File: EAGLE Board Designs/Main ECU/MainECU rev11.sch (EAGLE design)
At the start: 208 parts, among them J1 CONNECTOR-40__, J2 ADIS16460, J3 CONNECTOR-40__, J4 CONNECTOR-40__, J5 CONNECTOR-40__, K1 RELAY_DPDT_RT424024, K10 RELAY_DPDT_RT424024, K11 RELAY_DPDT_RT424024, K12 RELAY_DPDT_RT424024, K9 RELAY_DPDT_RT424024, Q3 TRANSISTOR_P_MOS_SOT-23_DMP30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, Q4 TRANSISTOR_N_MOS__DMG3406L-7, Q5 TRANSISTOR_P_MOS_SOT-23_DMP30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, Q6 TRANSISTOR_N_MOS__DMG3406L-7, U1 VOLTAGE_REGULATOR_SOT-223_3.3V, U2 TCAN1051HQV-Q1, U23 ADC128S022, U3 TCAN1051HQV-Q1, U32 ADC128S022, U33 TCAN1051HQV-Q1, U34 OPAMP_1_CHANNEL_OPA991, U37 OPAMP_1_CHANNEL_OPA991, U38 LOGICGATE_OR, U39 OPAMP_1_CHANNEL_OPA991, U4 TCAN1051HQV-Q1, U41 OPAMP_1_CHANNEL_OPA991, U42 LOGICGATE_OR, U43 OPAMP_1_CHANNEL_OPA991, U44 LOGICGATE_NAND, U45 TCAN1051HQV-Q1, U46 TCAN1051HQV-Q1, U5 ADM8316WBX30, U6 ADC128S022, U7 ADC128S022

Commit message: everything except LEDs
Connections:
- new net !AD4_CS: A3.D33, U32.!CS!
- net !AD3_CS: no longer A3.(CS)D10, U32.!CS!
- net +24V: now also J1.15, J1.16; no longer J1.1, J1.2
- net +5V: now also J1.14; no longer J1.3, J1.4
- net CANH_1: now also J1.12; no longer J1.16
- net CANH_2: now also J1.8; no longer J1.12
- net CANH_3: now also J1.4; no longer J1.8
- net CANL_1: now also J1.10; no longer J1.14
- net CANL_2: now also J1.6; no longer J1.10
- net CANL_3: now also J1.2; no longer J1.6
- net GND: now also J1.1, J1.3, J3.3, J3.4; no longer J1.15
- net REFERENCE: now also U32.IN2
- net SHDN_F: now also J3.1, J3.2
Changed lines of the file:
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@@
 <attribute name="DESCRIPTION_2" x="176.53" y="10.16" size="2.54" layer="95"/>
 </instance>
-<instance part="U$8" gate="G$1" x="43.18" y="203.2" smashed="yes">
-<attribute name="VALUE" x="43.18" y="208.28" size="1.778" layer="96" align="bottom-center"/>
+<instance part="U$8" gate="G$1" x="73.66" y="167.64" smashed="yes">
+<attribute name="VALUE" x="73.66" y="172.72" size="1.778" layer="96" align="bottom-center"/>
 </instance>
 <instance part="P46" gate="1" x="160.02" y="203.2" smashed="yes">
@@
 <attribute name="VALUE" x="137.16" y="92.71" size="1.27" layer="96" align="top-center"/>
 </instance>
-<instance part="P70" gate="1" x="48.26" y="203.2" smashed="yes">
-<attribute name="VALUE" x="48.26" y="205.74" size="1.27" layer="96" align="bottom-center"/>
+<instance part="P70" gate="1" x="68.58" y="170.18" smashed="yes">
+<attribute name="VALUE" x="68.58" y="172.72" size="1.27" layer="96" align="bottom-center"/>
 </instance>
 <instance part="J1" gate="G$1" x="30.48" y="200.66" smashed="yes">
@@
 <wire x1="78.74" y1="177.8" x2="78.74" y2="172.72" width="0.1524" layer="91"/>
 <wire x1="78.74" y1="172.72" x2="78.74" y2="167.64" width="0.1524" layer="91"/>
-<wire x1="78.74" y1="167.64" x2="78.74" y2="162.56" width="0.1524" layer="91"/>
-<wire x1="78.74" y1="162.56" x2="78.74" y2="157.48" width="0.1524" layer="91"/>
+<wire x1="78.74" y1="167.64" x2="78.74" y2="157.48" width="0.1524" layer="91"/>
 <wire x1="40.64" y1="182.88" x2="78.74" y2="182.88" width="0.1524" layer="91"/>
 <junction x="78.74" y="182.88"/>
@@
 <wire x1="40.64" y1="167.64" x2="78.74" y2="167.64" width="0.1524" layer="91"/>
 <junction x="78.74" y="167.64"/>
-<pinref part="J1" gate="G$1" pin="15"/>
-<wire x1="40.64" y1="162.56" x2="78.74" y2="162.56" width="0.1524" layer="91"/>
-<junction x="78.74" y="162.56"/>
+<pinref part="J1" gate="G$1" pin="1"/>
+<wire x1="40.64" y1="198.12" x2="78.74" y2="198.12" width="0.1524" layer="91"/>
+<wire x1="78.74" y1="198.12" x2="78.74" y2="193.04" width="0.1524" layer="91"/>
+<junction x="78.74" y="187.96"/>
+<pinref part="J1" gate="G$1" pin="3"/>
+<wire x1="78.74" y1="193.04" x2="78.74" y2="187.96" width="0.1524" layer="91"/>
+<wire x1="40.64" y1="193.04" x2="78.74" y2="193.04" width="0.1524" layer="91"/>
+<junction x="78.74" y="193.04"/>
 </segment>
 <segment>
 <pinref part="P68" gate="1" pin="GND"/>
-<wire x1="137.16" y1="187.96" x2="137.16" y2="137.16" width="0.1524" layer="91"/>
 <pinref part="J3" gate="G$1" pin="36"/>
 <wire x1="137.16" y1="137.16" x2="137.16" y2="134.62" width="0.1524" layer="91"/>
@@
 <pinref part="J3" gate="G$1" pin="25"/>
 <wire x1="99.06" y1="137.16" x2="137.16" y2="137.16" width="0.1524" layer="91"/>
+<pinref part="J3" gate="G$1" pin="3"/>
+<wire x1="99.06" y1="193.04" x2="137.16" y2="193.04" width="0.1524" layer="91"/>
+<wire x1="137.16" y1="193.04" x2="137.16" y2="190.5" width="0.1524" layer="91"/>
 <junction x="137.16" y="137.16"/>
+<pinref part="J3" gate="G$1" pin="4"/>
+<wire x1="137.16" y1="190.5" x2="137.16" y2="137.16" width="0.1524" layer="91"/>
+<wire x1="99.06" y1="190.5" x2="137.16" y2="190.5" width="0.1524" layer="91"/>
+<junction x="137.16" y="190.5"/>
 </segment>
 <segment>
@@
 <net name="CANH_1" class="0">
 <segment>
-<wire x1="40.64" y1="160.02" x2="48.26" y2="160.02" width="0.1524" layer="91"/>
-<label x="48.26" y="160.02" size="1.27" layer="95" xref="yes"/>
-<pinref part="J1" gate="G$1" pin="16"/>
-</segment>
-</net>
-<net name="CANL_1" class="0">
-<segment>
-<wire x1="40.64" y1="165.1" x2="48.26" y2="165.1" width="0.1524" layer="91"/>
-<label x="48.26" y="165.1" size="1.27" layer="95" xref="yes"/>
-<pinref part="J1" gate="G$1" pin="14"/>
-</segment>
-</net>
-<net name="CANH_2" class="0">
-<segment>
 <wire x1="40.64" y1="170.18" x2="48.26" y2="170.18" width="0.1524" layer="91"/>
 <label x="48.26" y="170.18" size="1.27" layer="95" xref="yes"/>
@@
 </segment>
 </net>
-<net name="CANL_2" class="0">
+<net name="CANL_1" class="0">
 <segment>
 <wire x1="40.64" y1="175.26" x2="48.26" y2="175.26" width="0.1524" layer="91"/>
@@
 </segment>
 </net>
-<net name="CANH_3" class="0">
+<net name="CANH_2" class="0">
 <segment>
 <wire x1="40.64" y1="180.34" x2="48.26" y2="180.34" width="0.1524" layer="91"/>
@@
 </segment>
 </net>
-<net name="CANL_3" class="0">
+<net name="CANL_2" class="0">
 <segment>
 <wire x1="40.64" y1="185.42" x2="48.26" y2="185.42" width="0.1524" layer="91"/>
@@
 </segment>
 </net>
+<net name="CANH_3" class="0">
+<segment>
+<wire x1="40.64" y1="190.5" x2="48.26" y2="190.5" width="0.1524" layer="91"/>
+<label x="48.26" y="190.5" size="1.27" layer="95" xref="yes"/>
+<pinref part="J1" gate="G$1" pin="4"/>
+</segment>
+</net>
+<net name="CANL_3" class="0">
+<segment>
+<wire x1="40.64" y1="195.58" x2="48.26" y2="195.58" width="0.1524" layer="91"/>
+<label x="48.26" y="195.58" size="1.27" layer="95" xref="yes"/>
+<pinref part="J1" gate="G$1" pin="2"/>
+</segment>
+</net>
 <net name="OKHS_IN" class="0">
 <segment>
@@
 </segment>
 <segment>
-<pinref part="J1" gate="G$1" pin="3"/>
 <pinref part="P70" gate="1" pin="+5V"/>
-<wire x1="40.64" y1="193.04" x2="48.26" y2="193.04" width="0.1524" layer="91"/>
-<wire x1="48.26" y1="193.04" x2="48.26" y2="200.66" width="0.1524" layer="91"/>
-<pinref part="J1" gate="G$1" pin="4"/>
-<wire x1="40.64" y1="190.5" x2="48.26" y2="190.5" width="0.1524" layer="91"/>
-<wire x1="48.26" y1="190.5" x2="48.26" y2="193.04" width="0.1524" layer="91"/>
-<junction x="48.26" y="193.04"/>
+<pinref part="J1" gate="G$1" pin="14"/>
+<wire x1="68.58" y1="165.1" x2="68.58" y2="167.64" width="0.1524" layer="91"/>
+<wire x1="40.64" y1="165.1" x2="68.58" y2="165.1" width="0.1524" layer="91"/>
 </segment>
 </net>
@@
 <net name="+24V" class="0">
 <segment>
-<pinref part="J1" gate="G$1" pin="2"/>
 <pinref part="U$8" gate="G$1" pin="+24V"/>
-<wire x1="40.64" y1="195.58" x2="43.18" y2="195.58" width="0.1524" layer="91"/>
-<wire x1="43.18" y1="195.58" x2="43.18" y2="198.12" width="0.1524" layer="91"/>
-<pinref part="J1" gate="G$1" pin="1"/>
-<wire x1="43.18" y1="198.12" x2="43.18" y2="200.66" width="0.1524" layer="91"/>
-<wire x1="40.64" y1="198.12" x2="43.18" y2="198.12" width="0.1524" layer="91"/>
-<junction x="43.18" y="198.12"/>
+<wire x1="73.66" y1="160.02" x2="73.66" y2="162.56" width="0.1524" layer="91"/>
+<pinref part="J1" gate="G$1" pin="15"/>
+<wire x1="73.66" y1="162.56" x2="73.66" y2="165.1" width="0.1524" layer="91"/>
+<wire x1="40.64" y1="162.56" x2="73.66" y2="162.56" width="0.1524" layer="91"/>
+<junction x="73.66" y="162.56"/>
+<pinref part="J1" gate="G$1" pin="16"/>
+<wire x1="40.64" y1="160.02" x2="73.66" y2="160.02" width="0.1524" layer="91"/>
 </segment>
 </net>
 <net name="SHDN_F" class="0">
 <segment>
-<wire x1="73.66" y1="205.74" x2="76.2" y2="205.74" width="0.1524" layer="91"/>
-<wire x1="73.66" y1="208.28" x2="76.2" y2="208.28" width="0.1524" layer="91"/>
-<wire x1="76.2" y1="208.28" x2="78.74" y2="208.28" width="0.1524" layer="91"/>
-<wire x1="76.2" y1="205.74" x2="76.2" y2="208.28" width="0.1524" layer="91"/>
-<junction x="76.2" y="208.28"/>
-<label x="78.74" y="208.28" size="1.27" layer="95" xref="yes"/>
+<wire x1="99.06" y1="195.58" x2="101.6" y2="195.58" width="0.1524" layer="91"/>
+<wire x1="99.06" y1="198.12" x2="101.6" y2="198.12" width="0.1524" layer="91"/>
+<wire x1="101.6" y1="198.12" x2="104.14" y2="198.12" width="0.1524" layer="91"/>
+<wire x1="101.6" y1="195.58" x2="101.6" y2="198.12" width="0.1524" layer="91"/>
+<junction x="101.6" y="198.12"/>
+<label x="104.14" y="198.12" size="1.27" layer="95" xref="yes"/>
+<pinref part="J3" gate="G$1" pin="1"/>
+<pinref part="J3" gate="G$1" pin="2"/>
 </segment>
 </net>
@@
 </segment>
 </net>
-<net name="!AD3_CS" class="0">
-<segment>
-<pinref part="A3" gate="G$1" pin="(CS)D10"/>
-<wire x1="60.96" y1="119.38" x2="68.58" y2="119.38" width="0.1524" layer="91"/>
-<label x="68.58" y="119.38" size="1.27" layer="95" xref="yes"/>
-</segment>
-<segment>
-<pinref part="U32" gate="G$1" pin="!CS!"/>
-<wire x1="226.06" y1="83.82" x2="223.52" y2="83.82" width="0.1524" layer="91"/>
-<label x="223.52" y="83.82" size="1.27" layer="95" rot="R180" xref="yes"/>
-</segment>
-</net>
 <net name="TELEM_SDO" class="0">
 <segment>
@@
 </segment>
 </net>
+<net name="!AD4_CS" class="0">
+<segment>
+<pinref part="U32" gate="G$1" pin="!CS!"/>
+<wire x1="226.06" y1="83.82" x2="223.52" y2="83.82" width="0.1524" layer="91"/>
+<label x="223.52" y="83.82" size="1.27" layer="95" rot="R180" xref="yes"/>
+</segment>
+<segment>
+<wire x1="60.96" y1="157.48" x2="68.58" y2="157.48" width="0.1524" layer="91"/>
+<label x="68.58" y="157.48" size="1.27" layer="95" xref="yes"/>
+<pinref part="A3" gate="G$1" pin="D33"/>
+</segment>
+</net>
+<net name="REFERENCE" class="0">
+<segment>
+<pinref part="U32" gate="G$1" pin="IN2"/>
+<wire x1="251.46" y1="91.44" x2="254" y2="91.44" width="0.1524" layer="91"/>
+<label x="254" y="91.44" size="1.27" layer="95" xref="yes"/>
+</segment>
+</net>

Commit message: LEDs
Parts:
- removed D27: LED_0603_YELLOW, HyTechDevices:LED_0603_YELLOW
- removed R41: RESISTOR_0603_180, HyTechDevices:RESISTOR_0603_180
- added D47: LED_0603_RED, HyTechDevices:LED_0603_RED
- added R38: RESISTOR_0603_2K, HyTechDevices:RESISTOR_0603_2K
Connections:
- removed net N$57: D27.A, R41.2
- new net N$13: D47.A, R38.2
- net CURRENT_FAULT: no longer R41.1
- net GND: now also D47.C; no longer D27.C
- net SHDN_F: now also R38.1
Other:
- moved on the sheet: D19, D20, D26, R12, R13, R40

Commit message: fixed BSPD
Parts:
- U42: value LOGICGATE_OR -> LOGICGATE_AND_DCK3; device HyTechDevices:LOGICGATE_OR -> HyTechDevices:LOGICGATE_AND_DCK3
- U44: value LOGICGATE_NAND -> LOGICGATE_NOR; device HyTechDevices:LOGICGATE_NAND -> HyTechDevices:LOGICGATE_NOR
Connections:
- net CURRENT_FAULT renamed SIG_MISSING
- removed net BRAKE_FAULT: R40.1, U42A.OUT, U44A.IN2
- new net BSPD_FAULT: U42A.OUT, U44A.IN2
- net BRAKE_HIGH: now also R40.1
- net BRAKE_MISSING: now also U38A.IN1; no longer U42A.IN2
- net CURRENT_HIGH: now also U42A.IN2; no longer U38A.IN1
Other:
- note removed: "curent out of range or signal missing"
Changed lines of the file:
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@@
 <part name="P242" library="HyTechSupplies" deviceset="GND" device=""/>
 <part name="P243" library="HyTechSupplies" deviceset="+5V" device=""/>
-<part name="U42" library="HyTechDevices" deviceset="LOGICGATE_OR" device=""/>
+<part name="U42" library="HyTechDevices" deviceset="LOGICGATE_AND_" device="" technology="DCK3"/>
 <part name="P244" library="HyTechSupplies" deviceset="+5V" device=""/>
 <part name="P245" library="HyTechSupplies" deviceset="GND" device=""/>
-<part name="U44" library="HyTechDevices" deviceset="LOGICGATE_NAND" device=""/>
+<part name="U44" library="HyTechDevices" deviceset="LOGICGATE_NOR" device=""/>
 <part name="P250" library="HyTechSupplies" deviceset="+5V" device=""/>
 <part name="P251" library="HyTechSupplies" deviceset="GND" device=""/>
@@
 CAN_2 - Rear-wheel inverters
 CAN_3 - Sensors and anything else</text>
-<text x="162.56" y="78.74" size="1.27" layer="97">curent out of range or signal missing</text>
 </plain>
 <instances>
@@
 </segment>
 </net>
-<net name="BRAKE_FAULT" class="0">
+<net name="N$13" class="0">
+<segment>
+<pinref part="D47" gate="LED" pin="A"/>
+<wire x1="190.5" y1="124.46" x2="187.96" y2="124.46" width="0.1524" layer="91"/>
+<pinref part="R38" gate="G$1" pin="2"/>
+</segment>
+</net>
+<net name="SHDN_F" class="0">
+<segment>
+<wire x1="180.34" y1="124.46" x2="177.8" y2="124.46" width="0.1524" layer="91"/>
+<label x="177.8" y="124.46" size="1.27" layer="95" rot="R180" xref="yes"/>
+<pinref part="R38" gate="G$1" pin="1"/>
+</segment>
+</net>
+<net name="BRAKE_HIGH" class="0">
 <segment>
 <pinref part="R40" gate="G$1" pin="1"/>
 <wire x1="180.34" y1="83.82" x2="177.8" y2="83.82" width="0.1524" layer="91"/>
 <label x="177.8" y="83.82" size="1.27" layer="95" rot="R180" xref="yes"/>
-</segment>
-</net>
-<net name="N$13" class="0">
-<segment>
-<pinref part="D47" gate="LED" pin="A"/>
-<wire x1="190.5" y1="124.46" x2="187.96" y2="124.46" width="0.1524" layer="91"/>
-<pinref part="R38" gate="G$1" pin="2"/>
-</segment>
-</net>
-<net name="SHDN_F" class="0">
-<segment>
-<wire x1="180.34" y1="124.46" x2="177.8" y2="124.46" width="0.1524" layer="91"/>
-<label x="177.8" y="124.46" size="1.27" layer="95" rot="R180" xref="yes"/>
-<pinref part="R38" gate="G$1" pin="1"/>
 </segment>
 </net>
@@
 </segment>
 <segment>
-<pinref part="U38" gate="A" pin="IN1"/>
-<wire x1="226.06" y1="106.68" x2="223.52" y2="106.68" width="0.1524" layer="91"/>
-<label x="223.52" y="106.68" size="1.27" layer="95" rot="R180" xref="yes"/>
+<wire x1="226.06" y1="76.2" x2="223.52" y2="76.2" width="0.1524" layer="91"/>
+<label x="223.52" y="76.2" size="1.27" layer="95" rot="R180" xref="yes"/>
+<pinref part="U42" gate="A" pin="IN2"/>
 </segment>
 </net>
@@
 </segment>
 <segment>
-<pinref part="U38" gate="A" pin="IN2"/>
 <wire x1="226.06" y1="101.6" x2="223.52" y2="101.6" width="0.1524" layer="91"/>
 <label x="223.52" y="101.6" size="1.27" layer="95" rot="R180" xref="yes"/>
-</segment>
-</net>
-<net name="CURRENT_FAULT" class="0">
-<segment>
-<pinref part="U38" gate="A" pin="OUT"/>
-<wire x1="238.76" y1="104.14" x2="241.3" y2="104.14" width="0.1524" layer="91"/>
-<label x="241.3" y="104.14" size="1.27" layer="95" xref="yes"/>
-</segment>
-<segment>
-<pinref part="U44" gate="A" pin="IN1"/>
-<wire x1="60.96" y1="104.14" x2="58.42" y2="104.14" width="0.1524" layer="91"/>
-<label x="58.42" y="104.14" size="1.27" layer="95" rot="R180" xref="yes"/>
+<pinref part="U38" gate="A" pin="IN2"/>
 </segment>
 </net>
@@
 </segment>
 <segment>
-<pinref part="U42" gate="A" pin="IN2"/>
-<wire x1="226.06" y1="76.2" x2="223.52" y2="76.2" width="0.1524" layer="91"/>
-<label x="223.52" y="76.2" size="1.27" layer="95" rot="R180" xref="yes"/>
+<wire x1="226.06" y1="106.68" x2="223.52" y2="106.68" width="0.1524" layer="91"/>
+<label x="223.52" y="106.68" size="1.27" layer="95" rot="R180" xref="yes"/>
+<pinref part="U38" gate="A" pin="IN1"/>
 </segment>
 </net>
@@
 <wire x1="226.06" y1="81.28" x2="223.52" y2="81.28" width="0.1524" layer="91"/>
 <label x="223.52" y="81.28" size="1.27" layer="95" rot="R180" xref="yes"/>
-</segment>
-</net>
-<net name="BRAKE_FAULT" class="0">
-<segment>
-<pinref part="U42" gate="A" pin="OUT"/>
-<wire x1="238.76" y1="78.74" x2="241.3" y2="78.74" width="0.1524" layer="91"/>
-<label x="241.3" y="78.74" size="1.27" layer="95" xref="yes"/>
-</segment>
-<segment>
-<pinref part="U44" gate="A" pin="IN2"/>
-<wire x1="60.96" y1="99.06" x2="58.42" y2="99.06" width="0.1524" layer="91"/>
-<label x="58.42" y="99.06" size="1.27" layer="95" rot="R180" xref="yes"/>
 </segment>
 </net>
@@
 </segment>
 </net>
+<net name="SIG_MISSING" class="0">
+<segment>
+<pinref part="U38" gate="A" pin="OUT"/>
+<wire x1="238.76" y1="104.14" x2="241.3" y2="104.14" width="0.1524" layer="91"/>
+<label x="241.3" y="104.14" size="1.27" layer="95" xref="yes"/>
+</segment>
+<segment>
+<pinref part="U44" gate="A" pin="IN1"/>
+<wire x1="60.96" y1="104.14" x2="58.42" y2="104.14" width="0.1524" layer="91"/>
+<label x="58.42" y="104.14" size="1.27" layer="95" rot="R180" xref="yes"/>
+</segment>
+</net>
+<net name="BSPD_FAULT" class="0">
+<segment>
+<pinref part="U42" gate="A" pin="OUT"/>
+<wire x1="238.76" y1="78.74" x2="241.3" y2="78.74" width="0.1524" layer="91"/>
+<label x="241.3" y="78.74" size="1.27" layer="95" xref="yes"/>
+</segment>
+<segment>
+<pinref part="U44" gate="A" pin="IN2"/>
+<wire x1="60.96" y1="99.06" x2="58.42" y2="99.06" width="0.1524" layer="91"/>
+<label x="58.42" y="99.06" size="1.27" layer="95" rot="R180" xref="yes"/>
+</segment>
+</net>

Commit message: fixed DRC
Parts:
- XF2: value FUSE_HOLDER_MINIBLADEPTH -> FUSE_HOLDER_MINIBLADESMD; device HyTechDevices:FUSE_HOLDER_MINIBLADEPTH -> HyTechDevices:FUSE_HOLDER_MINIBLADESMD
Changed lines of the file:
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@@
 <part name="C3" library="HyTechDevices" deviceset="CAPACITOR_?_*" device="0603" technology="25V_10UF"/>
 <part name="C4" library="HyTechDevices" deviceset="CAPACITOR_?_*" device="0603" technology="25V_10UF"/>
-<part name="XF2" library="HyTechDevices" deviceset="FUSE_HOLDER_*" device="PTH" technology="MINIBLADE"/>
+<part name="XF2" library="HyTechDevices" deviceset="FUSE_HOLDER_*" device="SMD" technology="MINIBLADE" value="FUSE_HOLDER_MINIBLADESMD"/>
 <part name="U$3" library="HyTechSupplies" deviceset="+24V" device=""/>
 <part name="JP1" library="HyTechDevices" deviceset="JUMPER_?_*" device="" technology="1X02"/>

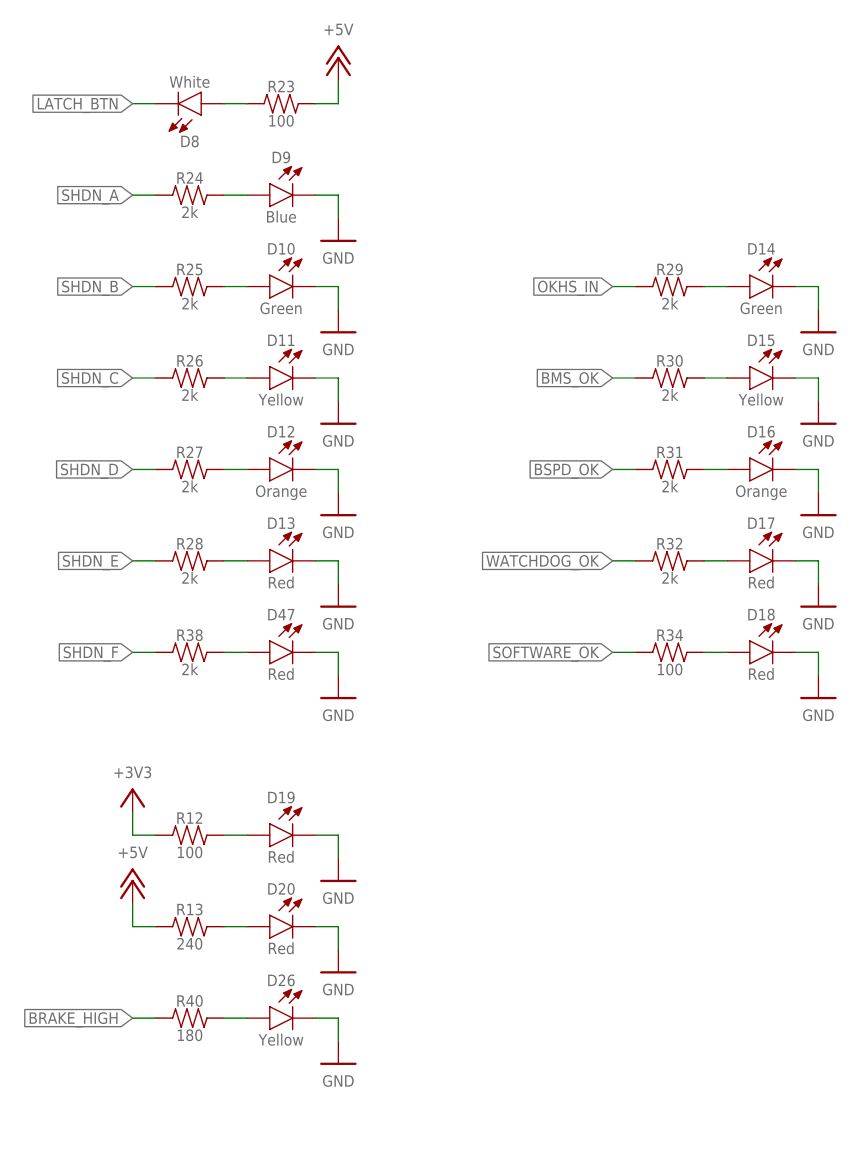
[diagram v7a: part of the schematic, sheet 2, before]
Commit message: LED text
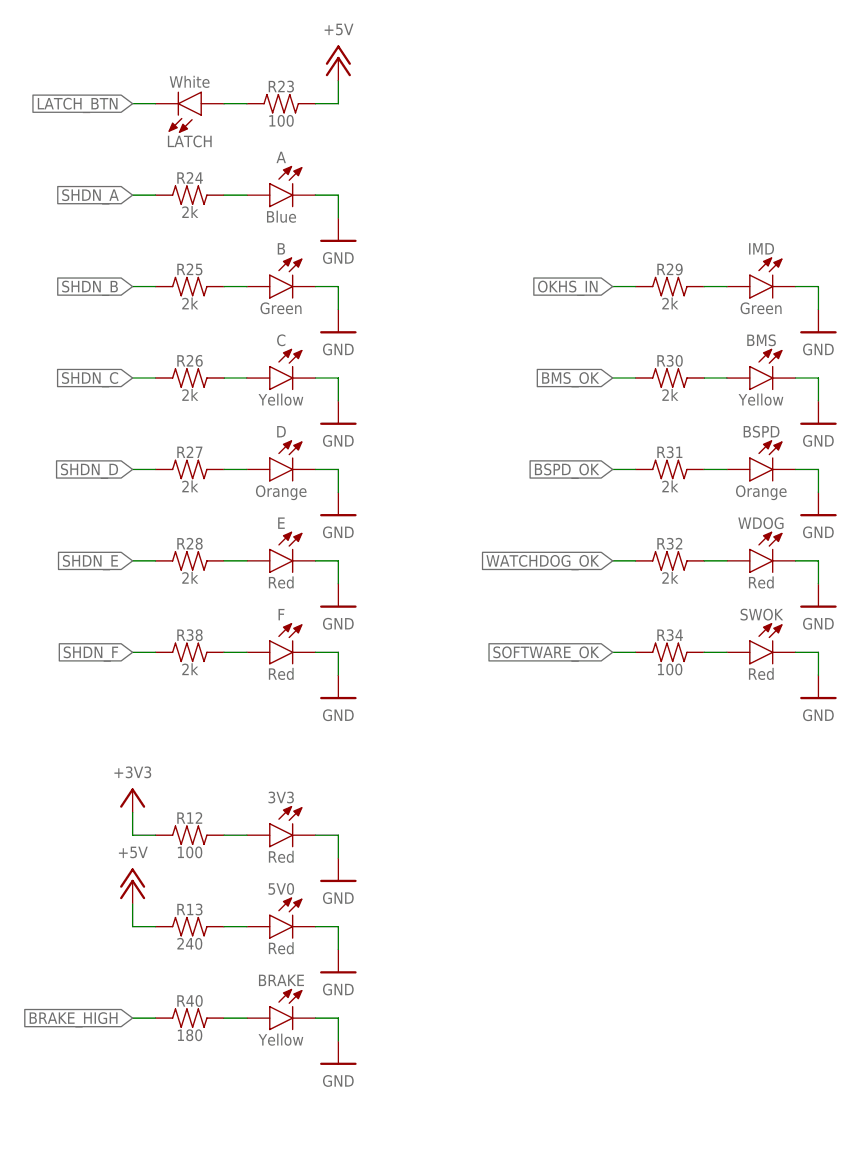
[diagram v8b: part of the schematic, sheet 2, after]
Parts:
- renumbered D10 to B, D11 to C, D12 to D, D13 to E, D14 to IMD, D15 to BMS, D16 to BSPD, D17 to WDOG, D18 to SWOK, D19 to 3V3, D20 to 5V0, D26 to BRAKE, D47 to F, D8 to LATCH, D9 to A
